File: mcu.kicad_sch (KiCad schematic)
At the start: 3 parts, among them J1 Conn_ARM_JTAG_SWD_20, U1 STM32F469AEHx

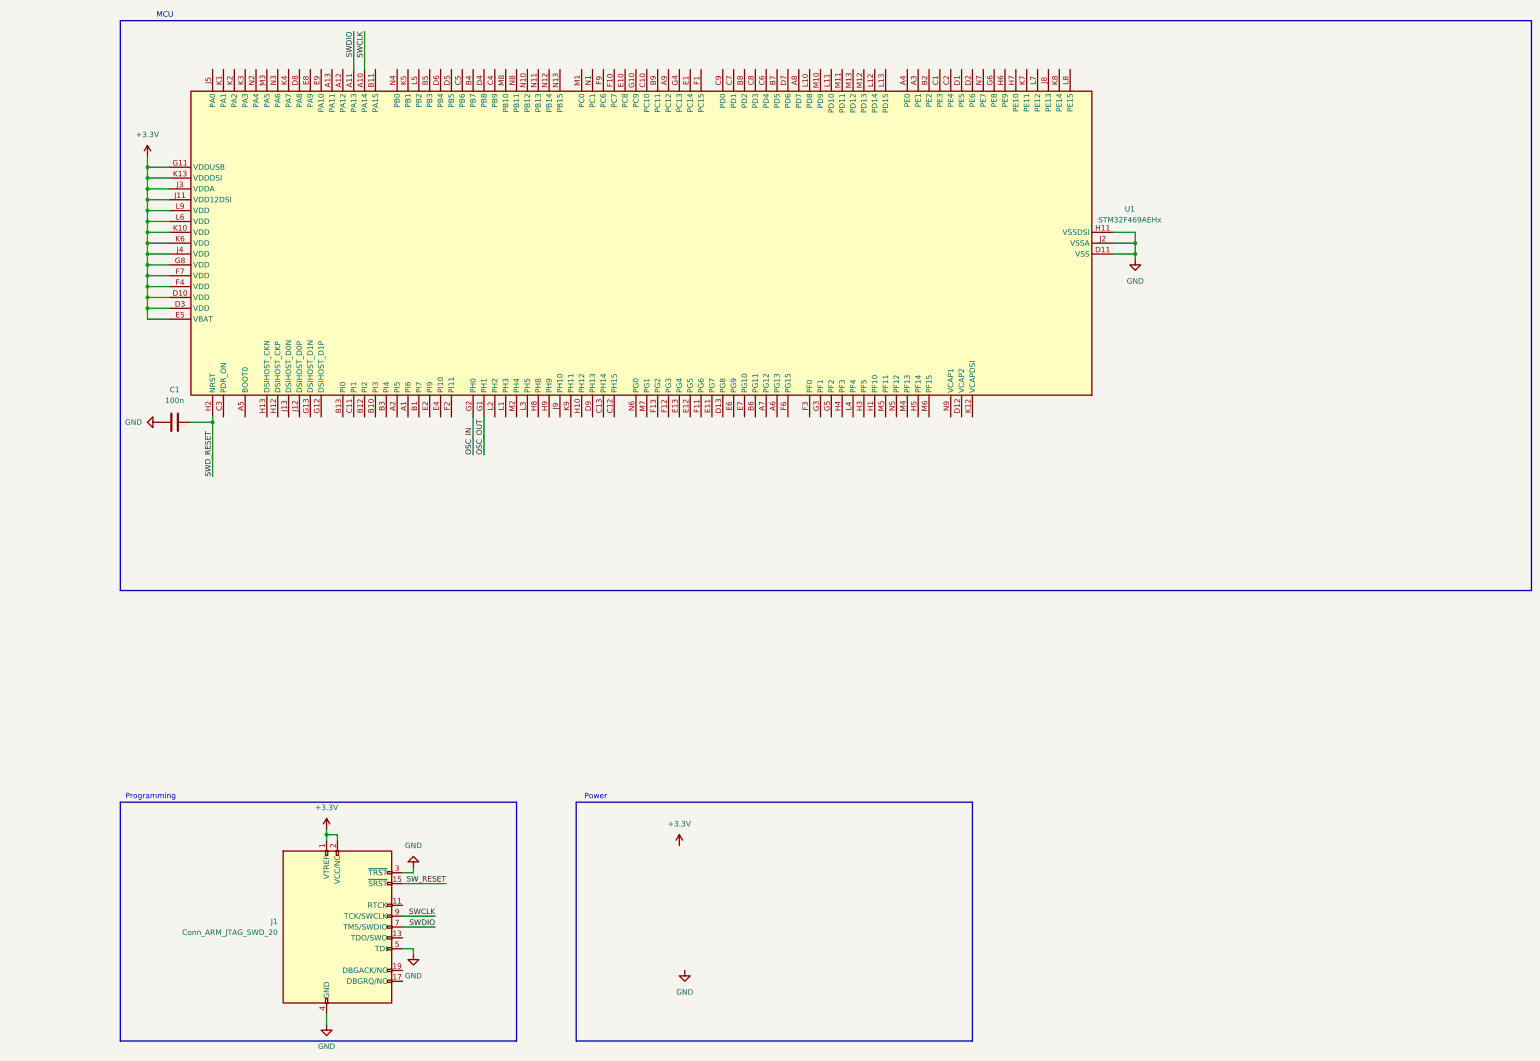
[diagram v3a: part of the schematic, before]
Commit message: added MCU decaps and hall effect schematic
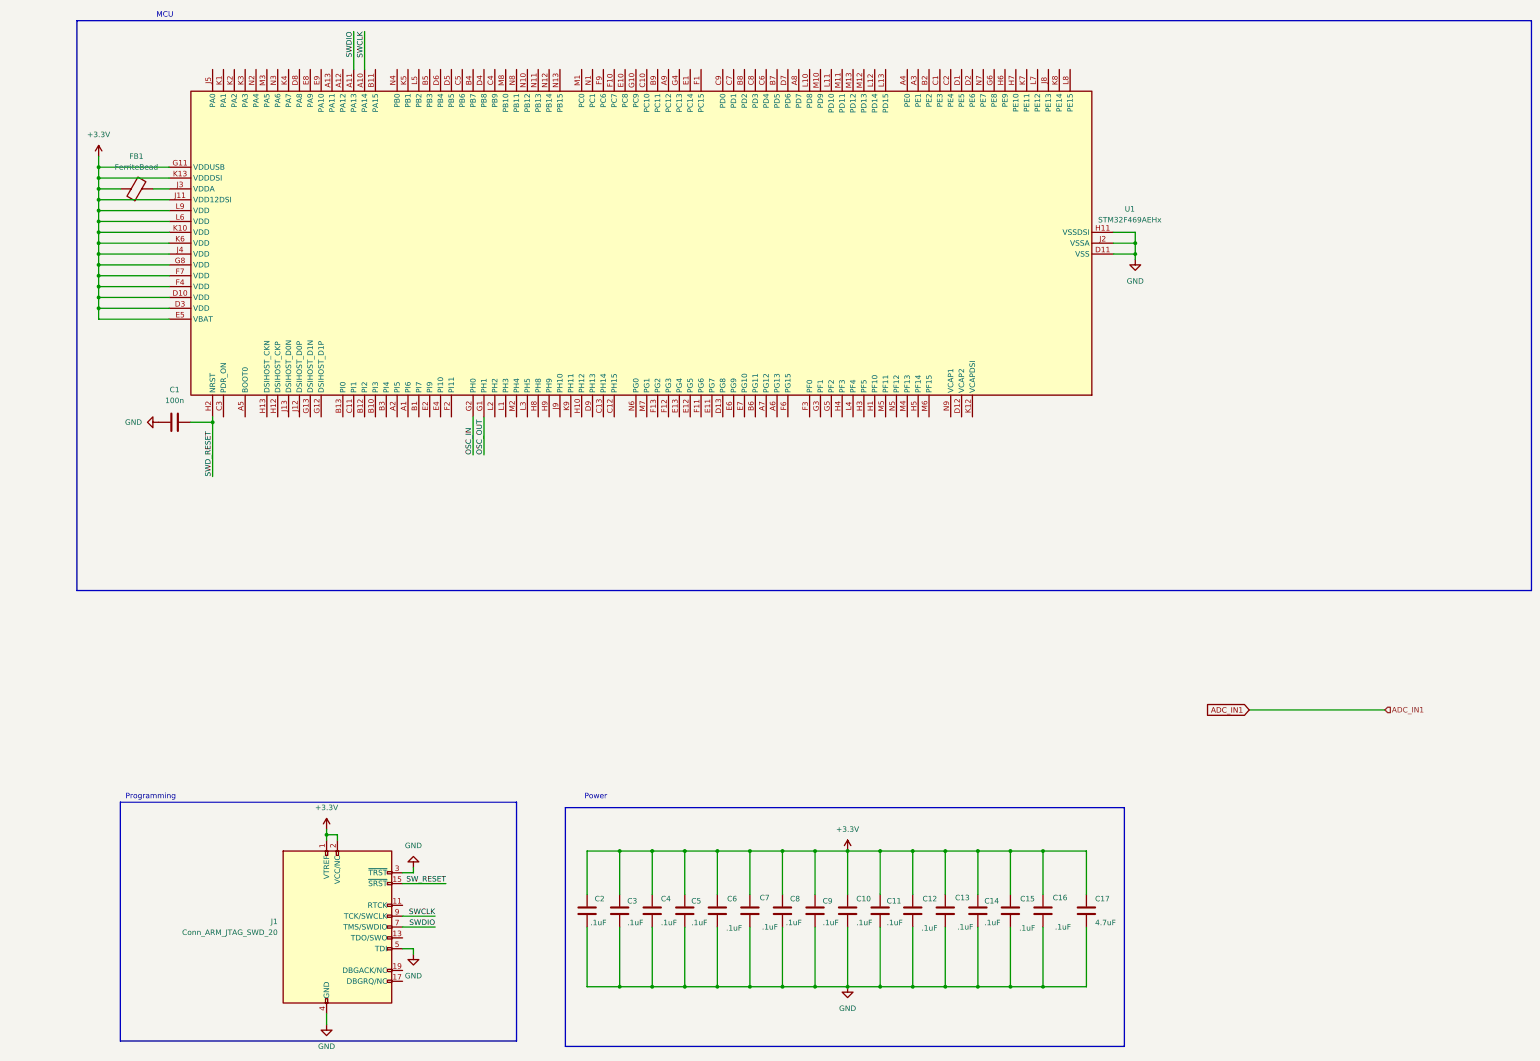
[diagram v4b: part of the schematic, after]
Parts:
- added C10, C11, C12, C13, C14, C15, C16, C2, C3, C4, C5, C6, C7, C8, C9: .1uF, symbol Device:C
- added C17: 4.7uF, symbol Device:C
- added FB1: FerriteBead, symbol Device:FerriteBead
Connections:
- net +3.3V: now also C10.1, C11.1, C12.1, C13.1, C14.1, C15.1, C16.1, C17.1, C2.1, C3.1, C4.1, C5.1, C6.1, C7.1, C8.1, C9.1, FB1.1; no longer U1.J3 (VDDA)
- net GND: now also C10.2, C11.2, C12.2, C13.2, C14.2, C15.2, C16.2, C17.2, C2.2, C3.2, C4.2, C5.2, C6.2, C7.2, C8.2, C9.2
- new net: FB1.2, U1.J3 (VDDA)

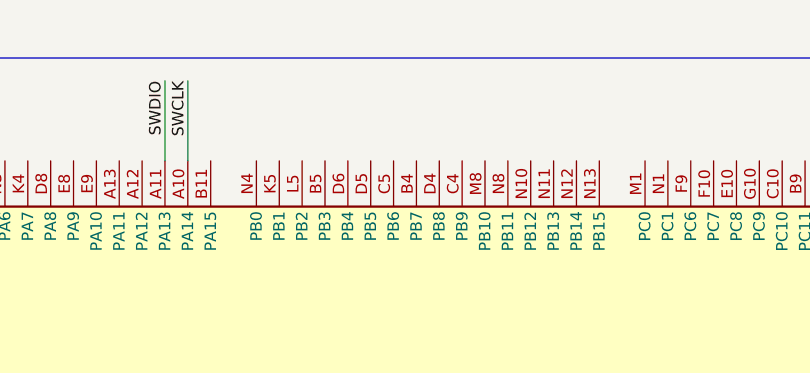
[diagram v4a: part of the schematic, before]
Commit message: Added footprint library for EEProm
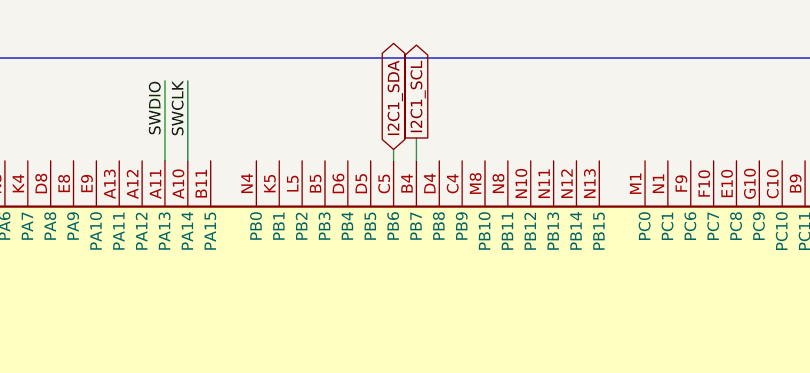
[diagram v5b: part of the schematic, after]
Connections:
- net I2C1_SCL: now reaches U1.B4 (PB7)
- net I2C1_SDA: now reaches U1.C5 (PB6)
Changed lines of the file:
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@@
+	(wire
+		(pts
+			(xy 110.49 40.64) (xy 110.49 41.91)
+		)
+		(stroke
+			(width 0)
+			(type default)
+		)
+	)
 	(wire
 		(pts
@@
 		(pts
 			(xy 25.4 64.77) (xy 25.4 62.23)
+		)
+		(stroke
+			(width 0)
+			(type default)
+		)
+	)
+	(wire
+		(pts
+			(xy 113.03 39.37) (xy 113.03 41.91)
 		)
 		(stroke
@@
 		)
 	)
+	(global_label "I2C1_SCL"
+		(shape output)
+		(at 113.03 39.37 90)
+		(fields_autoplaced yes)
+		(effects
+			(font
+				(size 1.27 1.27)
+			)
+			(justify left)
+		)
+		(property "Intersheetrefs" "${INTERSHEET_REFS}"
+			(at 113.03 27.6158 90)
+			(effects
+				(font
+					(size 1.27 1.27)
+				)
+				(justify left)
+				(hide yes)
+			)
+		)
+	)
+	(global_label "I2C1_SDA"
+		(shape bidirectional)
+		(at 110.49 40.64 90)
+		(fields_autoplaced yes)
+		(effects
+			(font
+				(size 1.27 1.27)
+			)
+			(justify left)
+		)
+		(property "Intersheetrefs" "${INTERSHEET_REFS}"
+			(at 110.49 27.714 90)
+			(effects
+				(font
+					(size 1.27 1.27)
+				)
+				(justify left)
+				(hide yes)
+			)
+		)
+	)
